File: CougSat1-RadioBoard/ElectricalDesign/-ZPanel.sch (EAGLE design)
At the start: 46 parts, among them J1 High Gain Antenna, J2 Deployables, J3 High Gain +, J4 ADCS, J5 Flap +X, J6 Flap -X, J7 Flap +Y, J8 Flap -Y, U1 AD7291, U3 AD8515

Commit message: Laid out RF
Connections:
- net HIGH_G_1 renamed COAX_CENTER
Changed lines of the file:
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@@
 <?xml version="1.0" encoding="utf-8"?>
 <!DOCTYPE eagle SYSTEM "eagle.dtd">
-<eagle version="9.5.2">
+<eagle version="9.5.1">
 <drawing>
 <settings>
@@
 <grid distance="0.1" unitdist="inch" unit="inch" style="lines" multiple="1" display="no" altdistance="0.01" altunitdist="inch" altunit="inch"/>
 <layers>
-<layer number="1" name="Top" color="4" fill="1" visible="no" active="no"/>
-<layer number="2" name="Route2" color="1" fill="3" visible="no" active="no"/>
-<layer number="3" name="Route3" color="4" fill="3" visible="no" active="no"/>
-<layer number="4" name="Route4" color="1" fill="4" visible="no" active="no"/>
-<layer number="5" name="Route5" color="4" fill="4" visible="no" active="no"/>
-<layer number="6" name="Route6" color="1" fill="8" visible="no" active="no"/>
-<layer number="7" name="Route7" color="4" fill="8" visible="no" active="no"/>
-<layer number="8" name="Route8" color="1" fill="2" visible="no" active="no"/>
-<layer number="9" name="Route9" color="4" fill="2" visible="no" active="no"/>
-<layer number="10" name="Route10" color="1" fill="7" visible="no" active="no"/>
-<layer number="11" name="Route11" color="4" fill="7" visible="no" active="no"/>
-<layer number="12" name="Route12" color="1" fill="5" visible="no" active="no"/>
-<layer number="13" name="Route13" color="4" fill="5" visible="no" active="no"/>
-<layer number="14" name="Route14" color="1" fill="6" visible="no" active="no"/>
-<layer number="15" name="Route15" color="4" fill="6" visible="no" active="no"/>
-<layer number="16" name="Bottom" color="1" fill="1" visible="no" active="no"/>
-<layer number="17" name="Pads" color="2" fill="1" visible="no" active="no"/>
-<layer number="18" name="Vias" color="2" fill="1" visible="no" active="no"/>
-<layer number="19" name="Unrouted" color="6" fill="1" visible="no" active="no"/>
-<layer number="20" name="Dimension" color="24" fill="1" visible="no" active="no"/>
-<layer number="21" name="tPlace" color="7" fill="1" visible="no" active="no"/>
-<layer number="22" name="bPlace" color="7" fill="1" visible="no" active="no"/>
-<layer number="23" name="tOrigins" color="15" fill="1" visible="no" active="no"/>
-<layer number="24" name="bOrigins" color="15" fill="1" visible="no" active="no"/>
-<layer number="25" name="tNames" color="7" fill="1" visible="no" active="no"/>
-<layer number="26" name="bNames" color="7" fill="1" visible="no" active="no"/>
-<layer number="27" name="tValues" color="7" fill="1" visible="no" active="no"/>
-<layer number="28" name="bValues" color="7" fill="1" visible="no" active="no"/>
+<layer number="1" name="Top" color="4" fill="1" visible="yes" active="no"/>
+<layer number="2" name="Route2" color="16" fill="1" visible="yes" active="no"/>
+<layer number="3" name="Route3" color="17" fill="1" visible="yes" active="no"/>
+<layer number="4" name="Route4" color="18" fill="1" visible="yes" active="no"/>
+<layer number="5" name="Route5" color="19" fill="1" visible="yes" active="no"/>
+<layer number="6" name="Route6" color="25" fill="1" visible="yes" active="no"/>
+<layer number="7" name="Route7" color="26" fill="1" visible="yes" active="no"/>
+<layer number="8" name="Route8" color="27" fill="1" visible="yes" active="no"/>
+<layer number="9" name="Route9" color="28" fill="1" visible="yes" active="no"/>
+<layer number="10" name="Route10" color="29" fill="1" visible="yes" active="no"/>
+<layer number="11" name="Route11" color="30" fill="1" visible="yes" active="no"/>
+<layer number="12" name="Route12" color="20" fill="1" visible="yes" active="no"/>
+<layer number="13" name="Route13" color="21" fill="1" visible="yes" active="no"/>
+<layer number="14" name="Route14" color="22" fill="1" visible="yes" active="no"/>
+<layer number="15" name="Route15" color="23" fill="1" visible="yes" active="no"/>
+<layer number="16" name="Bottom" color="1" fill="1" visible="yes" active="no"/>
+<layer number="17" name="Pads" color="2" fill="1" visible="yes" active="no"/>
+<layer number="18" name="Vias" color="2" fill="1" visible="yes" active="no"/>
+<layer number="19" name="Unrouted" color="6" fill="1" visible="yes" active="no"/>
+<layer number="20" name="Dimension" color="24" fill="1" visible="yes" active="no"/>
+<layer number="21" name="tPlace" color="7" fill="1" visible="yes" active="no"/>
+<layer number="22" name="bPlace" color="7" fill="1" visible="yes" active="no"/>
+<layer number="23" name="tOrigins" color="15" fill="1" visible="yes" active="no"/>
+<layer number="24" name="bOrigins" color="15" fill="1" visible="yes" active="no"/>
+<layer number="25" name="tNames" color="7" fill="1" visible="yes" active="no"/>
+<layer number="26" name="bNames" color="7" fill="1" visible="yes" active="no"/>
+<layer number="27" name="tValues" color="7" fill="1" visible="yes" active="no"/>
+<layer number="28" name="bValues" color="7" fill="1" visible="yes" active="no"/>
 <layer number="29" name="tStop" color="7" fill="3" visible="no" active="no"/>
 <layer number="30" name="bStop" color="7" fill="6" visible="no" active="no"/>
@@
 <layer number="35" name="tGlue" color="7" fill="4" visible="no" active="no"/>
 <layer number="36" name="bGlue" color="7" fill="5" visible="no" active="no"/>
-<layer number="37" name="tTest" color="7" fill="1" visible="no" active="no"/>
-<layer number="38" name="bTest" color="7" fill="1" visible="no" active="no"/>
+<layer number="37" name="tTest" color="7" fill="1" visible="yes" active="no"/>
+<layer number="38" name="bTest" color="7" fill="1" visible="yes" active="no"/>
 <layer number="39" name="tKeepout" color="4" fill="11" visible="no" active="no"/>
 <layer number="40" name="bKeepout" color="1" fill="11" visible="no" active="no"/>
@@
 <layer number="44" name="Drills" color="7" fill="1" visible="no" active="no"/>
 <layer number="45" name="Holes" color="7" fill="1" visible="no" active="no"/>
-<layer number="46" name="Milling" color="3" fill="1" visible="no" active="no"/>
-<layer number="47" name="Measures" color="7" fill="1" visible="no" active="no"/>
-<layer number="48" name="Document" color="7" fill="1" visible="no" active="no"/>
-<layer number="49" name="Reference" color="7" fill="1" visible="no" active="no"/>
-<layer number="50" name="dxf" color="7" fill="1" visible="no" active="no"/>
-<layer number="51" name="tDocu" color="7" fill="1" visible="no" active="no"/>
-<layer number="52" name="bDocu" color="7" fill="1" visible="no" active="no"/>
-<layer number="53" name="tGND_GNDA" color="7" fill="9" visible="no" active="no"/>
-<layer number="54" name="bGND_GNDA" color="1" fill="9" visible="no" active="no"/>
-<layer number="56" name="wert" color="7" fill="1" visible="no" active="no"/>
-<layer number="57" name="tCAD" color="7" fill="1" visible="no" active="no"/>
-<layer number="58" name="bCAD" color="9" fill="1" visible="no" active="no"/>
-<layer number="59" name="tCarbon" color="7" fill="1" visible="no" active="no"/>
-<layer number="60" name="bCarbon" color="7" fill="1" visible="no" active="no"/>
+<layer number="46" name="Milling" color="3" fill="1" visible="yes" active="no"/>
+<layer number="47" name="Measures" color="7" fill="1" visible="yes" active="no"/>
+<layer number="48" name="Document" color="7" fill="1" visible="yes" active="no"/>
+<layer number="49" name="Reference" color="7" fill="1" visible="yes" active="no"/>
+<layer number="50" name="dxf" color="7" fill="1" visible="yes" active="no"/>
+<layer number="51" name="tDocu" color="7" fill="1" visible="yes" active="no"/>
+<layer number="52" name="bDocu" color="7" fill="1" visible="yes" active="no"/>
+<layer number="53" name="tGND_GNDA" color="7" fill="9" visible="yes" active="no"/>
+<layer number="54" name="bGND_GNDA" color="1" fill="9" visible="yes" active="no"/>
+<layer number="56" name="wert" color="7" fill="1" visible="yes" active="no"/>
+<layer number="57" name="tCAD" color="7" fill="1" visible="yes" active="no"/>
+<layer number="58" name="bCAD" color="9" fill="1" visible="yes" active="no"/>
+<layer number="59" name="tCarbon" color="7" fill="1" visible="yes" active="no"/>
+<layer number="60" name="bCarbon" color="7" fill="1" visible="yes" active="no"/>
 <layer number="88" name="SimResults" color="9" fill="1" visible="yes" active="yes"/>
 <layer number="89" name="SimProbes" color="9" fill="1" visible="yes" active="yes"/>
@@
 <classes>
 <class number="0" name="default" width="0" drill="0">
+</class>
+<class number="1" name="RF" width="0" drill="0">
+<clearance class="1" value="1.65"/>
 </class>
 </classes>
@@
 </segment>
 </net>
-<net name="HIGH_G_1" class="0">
+<net name="COAX_CENTER" class="0">
 <segment>
 <pinref part="J3" gate="G$1" pin="1"/>

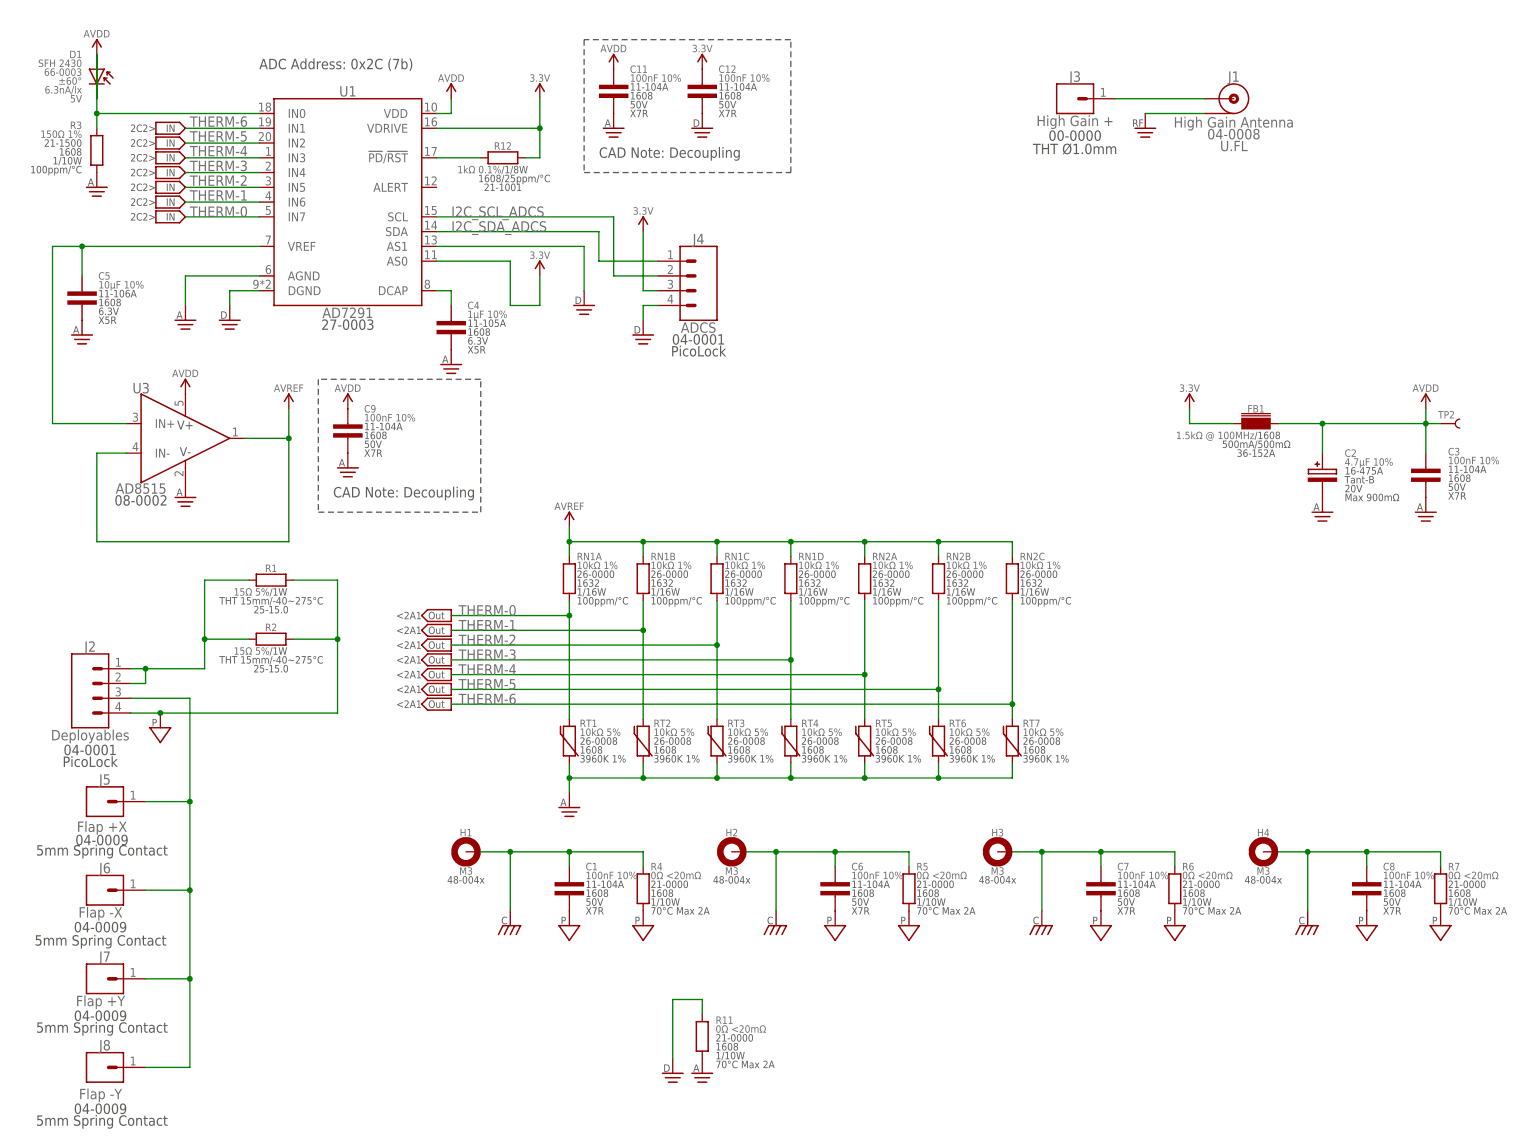
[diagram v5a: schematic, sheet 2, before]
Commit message: Ready for review
Ripped up RF traces
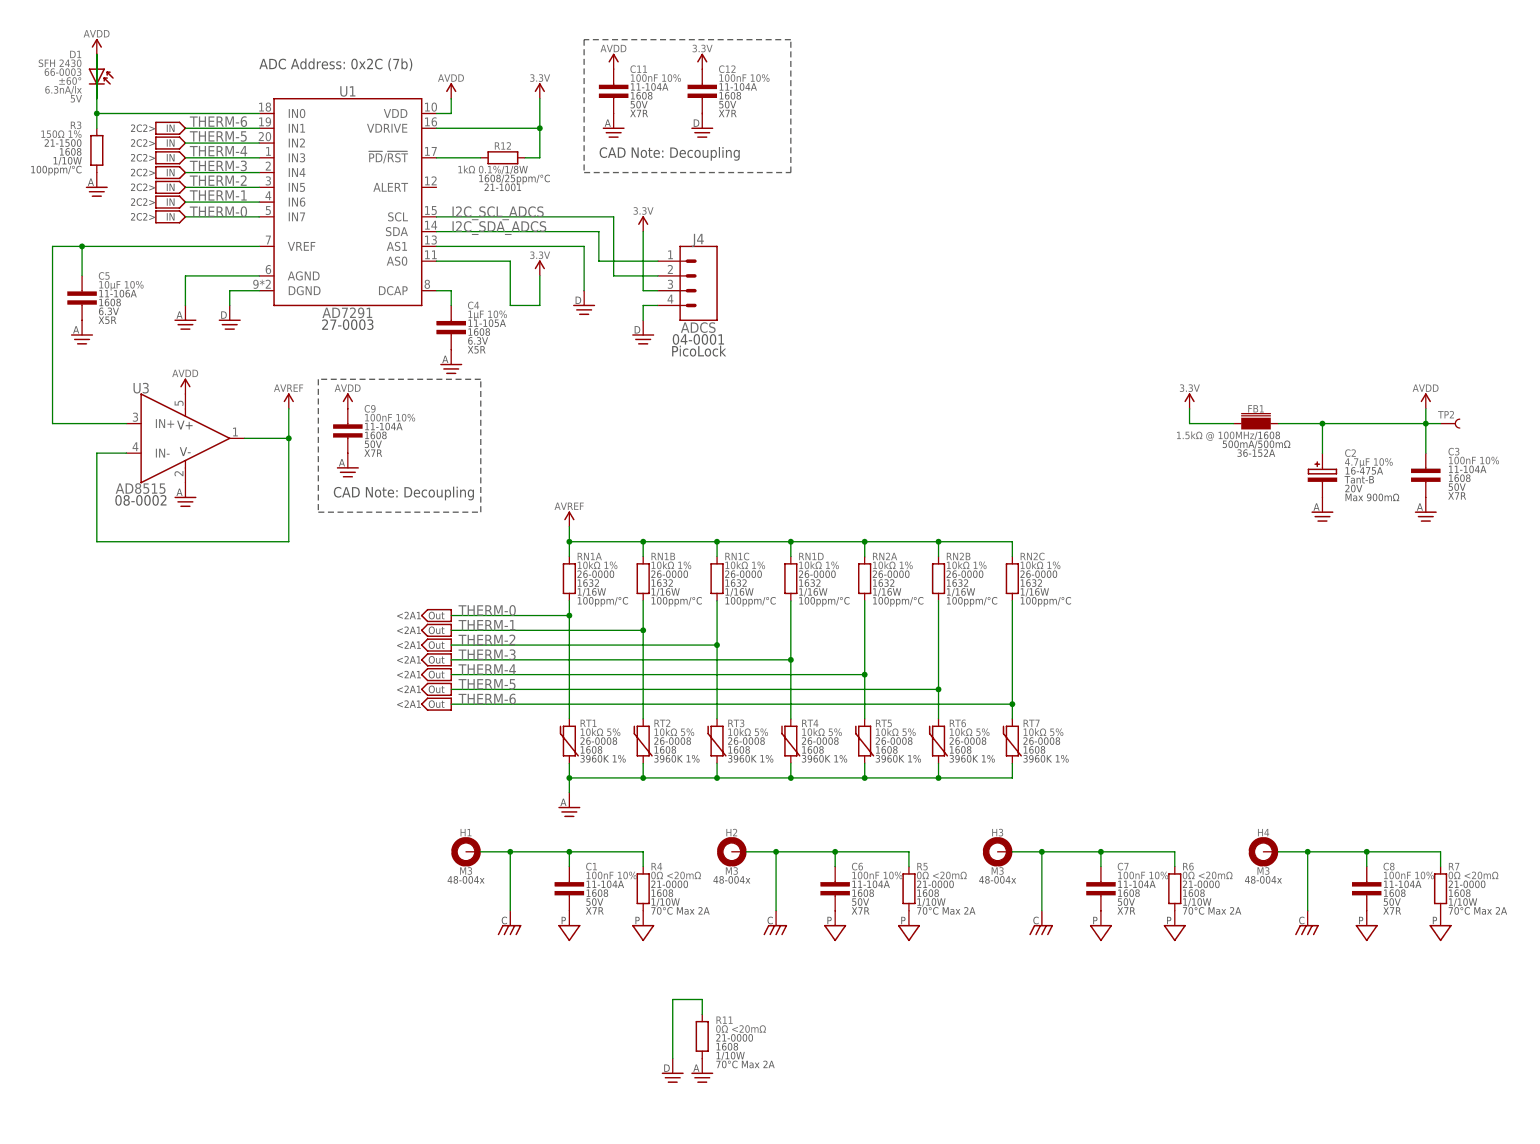
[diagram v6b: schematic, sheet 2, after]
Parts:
- removed J1: High Gain Antenna, CougsInSpace-Connectors:COAX-U.FL
- removed J2: Deployables, CougsInSpace-Connectors:1X04-PICOLOCK
- removed J3: High Gain +, CougsInSpace-Connectors:1X01-THT-1.0
- removed J5: Flap +X, CougsInSpace-Connectors:1X01-5MM-SPRING-0990
- removed J6: Flap -X, CougsInSpace-Connectors:1X01-5MM-SPRING-0990
- removed J7: Flap +Y, CougsInSpace-Connectors:1X01-5MM-SPRING-0990
- removed J8: Flap -Y, CougsInSpace-Connectors:1X01-5MM-SPRING-0990
- removed R1, R2: 15Ω 5%, CougsInSpace-Resistors:RES-H-15R-THT-15MM
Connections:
- removed net COAX_CENTER: J1.CENTER, J3.1
- removed net DEPLOY-H: J2.1, J2.2, R1.1, R2.1
- removed net RFGND: J1.SHIELD
- removed net SPRING_CONTACT: J2.3, J5.1, J6.1, J7.1, J8.1
- net PGND: no longer J2.4, R1.2, R2.2

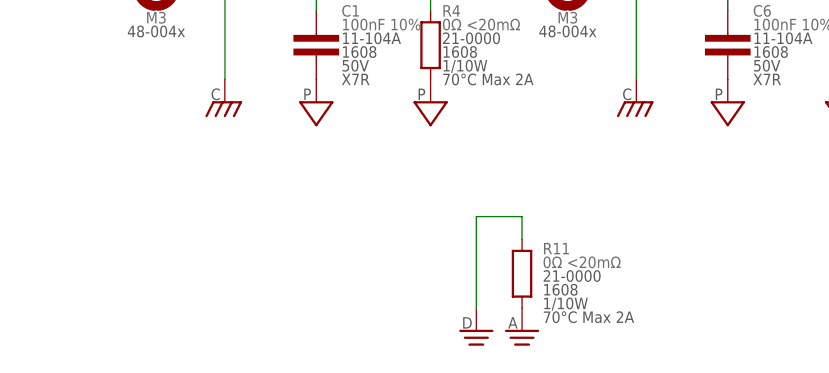
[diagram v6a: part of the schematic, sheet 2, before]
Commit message: Updated Layout Z
Updated minimizing VREF and adding R1 to connect DGND to PGND
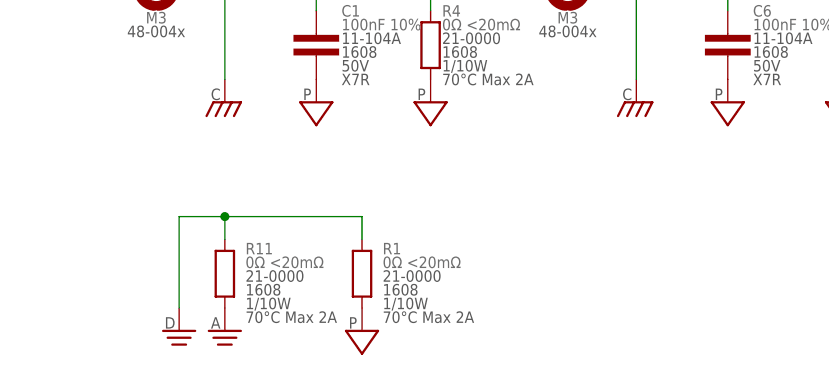
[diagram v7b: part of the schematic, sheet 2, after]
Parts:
- added R1: 0Ω <20mΩ, CougsInSpace-Resistors:RES-V-0-1608
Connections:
- net DGND: now also R1.2
- net PGND: now also R1.1
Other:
- moved on the sheet: R11
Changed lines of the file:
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@@
 <part name="SUPPLY42" library="CougsInSpace-PowerSymbols" deviceset="AGND" device=""/>
 <part name="SUPPLY13" library="CougsInSpace-PowerSymbols" deviceset="DGND" device=""/>
+<part name="R1" library="CougsInSpace-Resistors" deviceset="RES-V" device="-1608" technology="-0" value="0Ω &lt;20mΩ"/>
+<part name="SUPPLY3" library="CougsInSpace-PowerSymbols" deviceset="PGND" device=""/>
 </parts>
 <sheets>
@@
 <attribute name="VALUE" x="12.7" y="188.976" size="1.27" layer="96" align="center"/>
 </instance>
-<instance part="SUPPLY15" gate="1" x="111.76" y="10.16" smashed="yes"/>
-<instance part="SUPPLY16" gate="G$1" x="116.84" y="10.16" smashed="yes"/>
-<instance part="R11" gate="G$1" x="116.84" y="15.24" smashed="yes">
-<attribute name="NAME" x="119.126" y="19.304" size="1.27" layer="95" align="center-left"/>
-<attribute name="VALUE" x="119.126" y="17.78" size="1.27" layer="96" align="center-left"/>
-<attribute name="PACKAGE" x="119.126" y="14.732" size="1.27" layer="97" align="center-left"/>
-<attribute name="POWER" x="119.126" y="13.208" size="1.27" layer="97" align="center-left"/>
-<attribute name="TEMP" x="119.126" y="11.684" size="1.27" layer="97" align="center-left"/>
-<attribute name="SKU" x="119.126" y="16.256" size="1.27" layer="97" align="center-left"/>
+<instance part="SUPPLY15" gate="1" x="78.74" y="10.16" smashed="yes"/>
+<instance part="SUPPLY16" gate="G$1" x="83.82" y="10.16" smashed="yes"/>
+<instance part="R11" gate="G$1" x="83.82" y="15.24" smashed="yes">
+<attribute name="NAME" x="86.106" y="19.304" size="1.27" layer="95" align="center-left"/>
+<attribute name="VALUE" x="86.106" y="17.78" size="1.27" layer="96" align="center-left"/>
+<attribute name="PACKAGE" x="86.106" y="14.732" size="1.27" layer="97" align="center-left"/>
+<attribute name="POWER" x="86.106" y="13.208" size="1.27" layer="97" align="center-left"/>
+<attribute name="TEMP" x="86.106" y="11.684" size="1.27" layer="97" align="center-left"/>
+<attribute name="SKU" x="86.106" y="16.256" size="1.27" layer="97" align="center-left"/>
 </instance>
 <instance part="C2" gate="G$1" x="223.52" y="111.76" smashed="yes">
@@
 <instance part="SUPPLY42" gate="G$1" x="55.88" y="114.3" smashed="yes"/>
 <instance part="SUPPLY13" gate="1" x="106.68" y="137.16" smashed="yes"/>
+<instance part="R1" gate="G$1" x="99.06" y="15.24" smashed="yes">
+<attribute name="NAME" x="101.346" y="19.304" size="1.27" layer="95" align="center-left"/>
+<attribute name="VALUE" x="101.346" y="17.78" size="1.27" layer="96" align="center-left"/>
+<attribute name="PACKAGE" x="101.346" y="14.732" size="1.27" layer="97" align="center-left"/>
+<attribute name="POWER" x="101.346" y="13.208" size="1.27" layer="97" align="center-left"/>
+<attribute name="TEMP" x="101.346" y="11.684" size="1.27" layer="97" align="center-left"/>
+<attribute name="SKU" x="101.346" y="16.256" size="1.27" layer="97" align="center-left"/>
+</instance>
+<instance part="SUPPLY3" gate="G$1" x="99.06" y="10.16" smashed="yes"/>
 </instances>
 <busses>
@@
 </segment>
 <segment>
-<wire x1="111.76" y1="22.86" x2="116.84" y2="22.86" width="0.1524" layer="91"/>
+<wire x1="78.74" y1="22.86" x2="83.82" y2="22.86" width="0.1524" layer="91"/>
 <pinref part="R11" gate="G$1" pin="2"/>
-<wire x1="116.84" y1="22.86" x2="116.84" y2="20.32" width="0.1524" layer="91"/>
+<wire x1="83.82" y1="22.86" x2="83.82" y2="20.32" width="0.1524" layer="91"/>
 <pinref part="SUPPLY15" gate="1" pin="DGND"/>
-<wire x1="111.76" y1="22.86" x2="111.76" y2="12.7" width="0.1524" layer="91"/>
+<wire x1="78.74" y1="22.86" x2="78.74" y2="12.7" width="0.1524" layer="91"/>
+<pinref part="R1" gate="G$1" pin="2"/>
+<wire x1="83.82" y1="22.86" x2="99.06" y2="22.86" width="0.1524" layer="91"/>
+<wire x1="99.06" y1="22.86" x2="99.06" y2="20.32" width="0.1524" layer="91"/>
+<junction x="83.82" y="22.86"/>
 </segment>
 </net>
@@
 <pinref part="R7" gate="G$1" pin="1"/>
 </segment>
+<segment>
+<pinref part="R1" gate="G$1" pin="1"/>
+<pinref part="SUPPLY3" gate="G$1" pin="PGND"/>
+</segment>
 </net>

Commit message: Revised changes mentioned in PR
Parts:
- added TP1: TEST_POINT-THT-0.7, CougsInSpace-Connectors:TEST_POINT-THT-0.7
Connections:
- net THERM-0 renamed FRONT_TOP_LEFT
- net THERM-1 renamed FRONT_MIDDLE_LEFT
- net THERM-2 renamed FRONT_BOTTOM_LEFT
- net THERM-3 renamed FRONT_BOTTOM_MIDDLE
- net THERM-4 renamed FRONT_BOTTOM_RIGHT
- net THERM-5 renamed FRONT_MIDDLE_RIGHT
- net THERM-6 renamed FRONT_TOP_RIGHT
- net AGND: now also TP1.1
- net DGND: no longer J4.4
- net PGND: now also J4.4
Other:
- moved on the sheet: C2, C3, D1, FB1, TP2
